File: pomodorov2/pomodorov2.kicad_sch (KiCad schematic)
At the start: 5 parts, among them J1 Conn_ARM_JTAG_SWD_10, J2 TC2050-IDC, J3 Conn_01x08, U1 nRF52832-QFxx

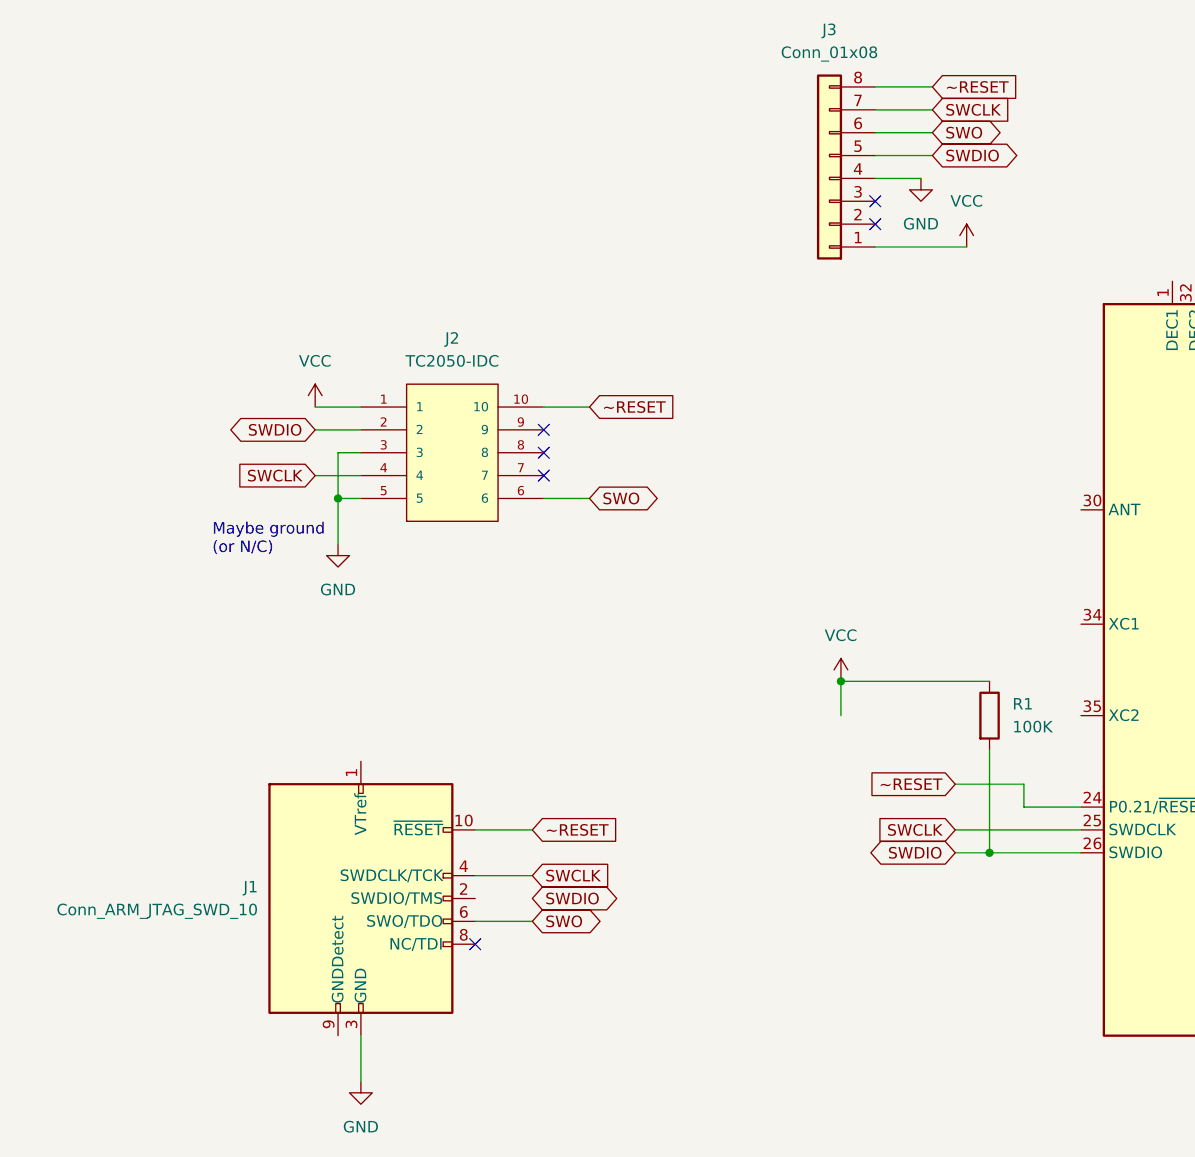
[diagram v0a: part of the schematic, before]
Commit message: Remove cortex header
- remove main cortex header
- tag-connect remains
- soicbite remains
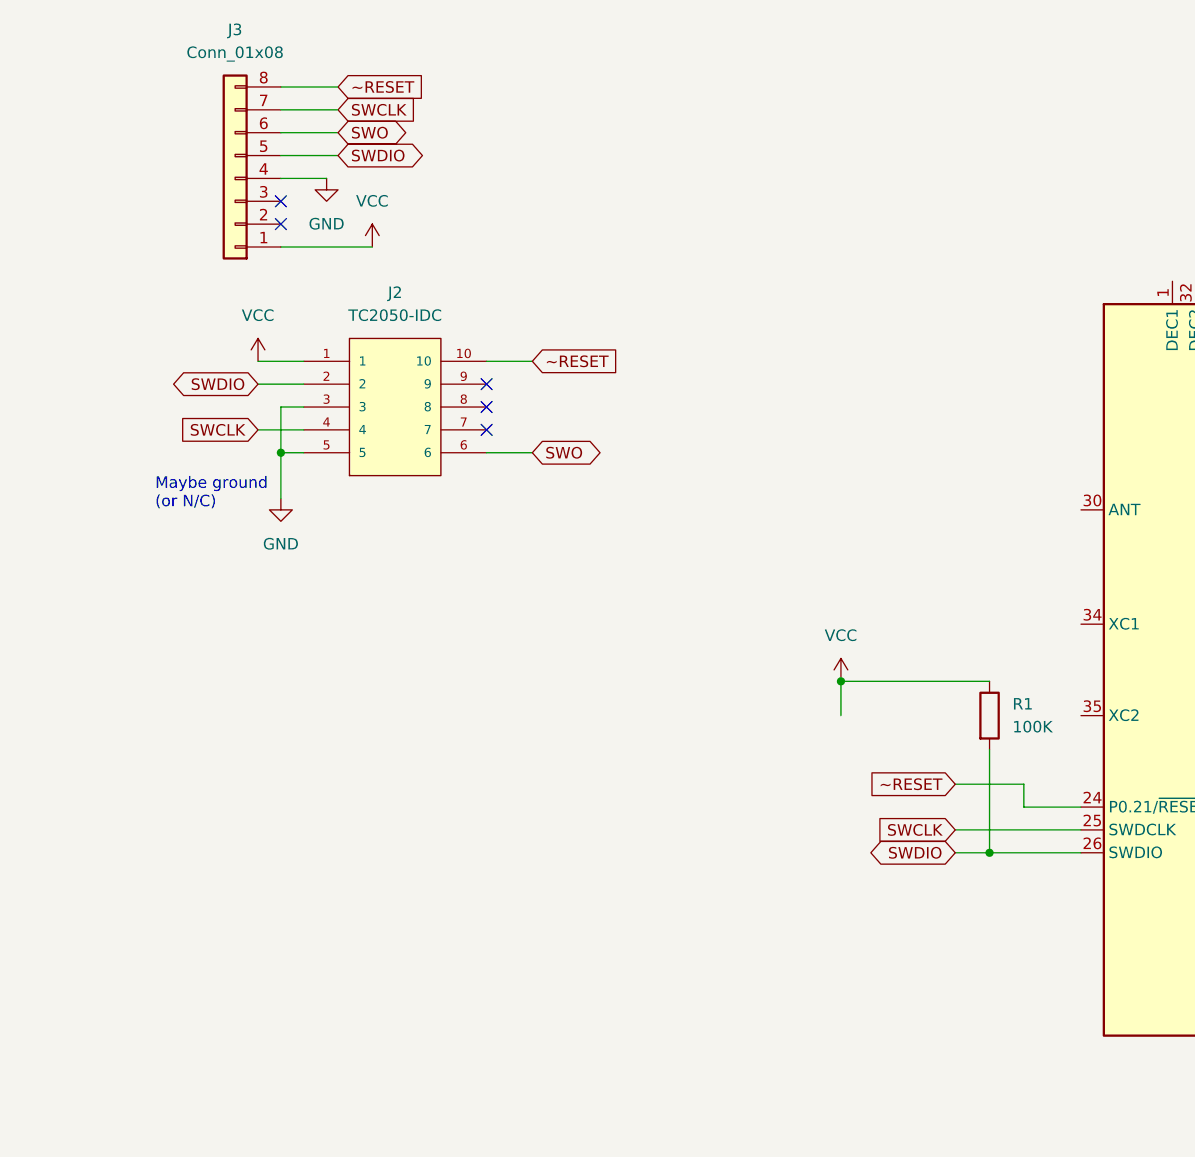
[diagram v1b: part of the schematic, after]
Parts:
- removed J1: Conn_ARM_JTAG_SWD_10, Connector_PinHeader_1.27mm:PinHeader_2x05_P1.27mm_Vertical_SMD, symbol Connector:Conn_ARM_JTAG_SWD_10
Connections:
- no-connect marks 6 -> 5
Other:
- moved on the sheet: J2, J3

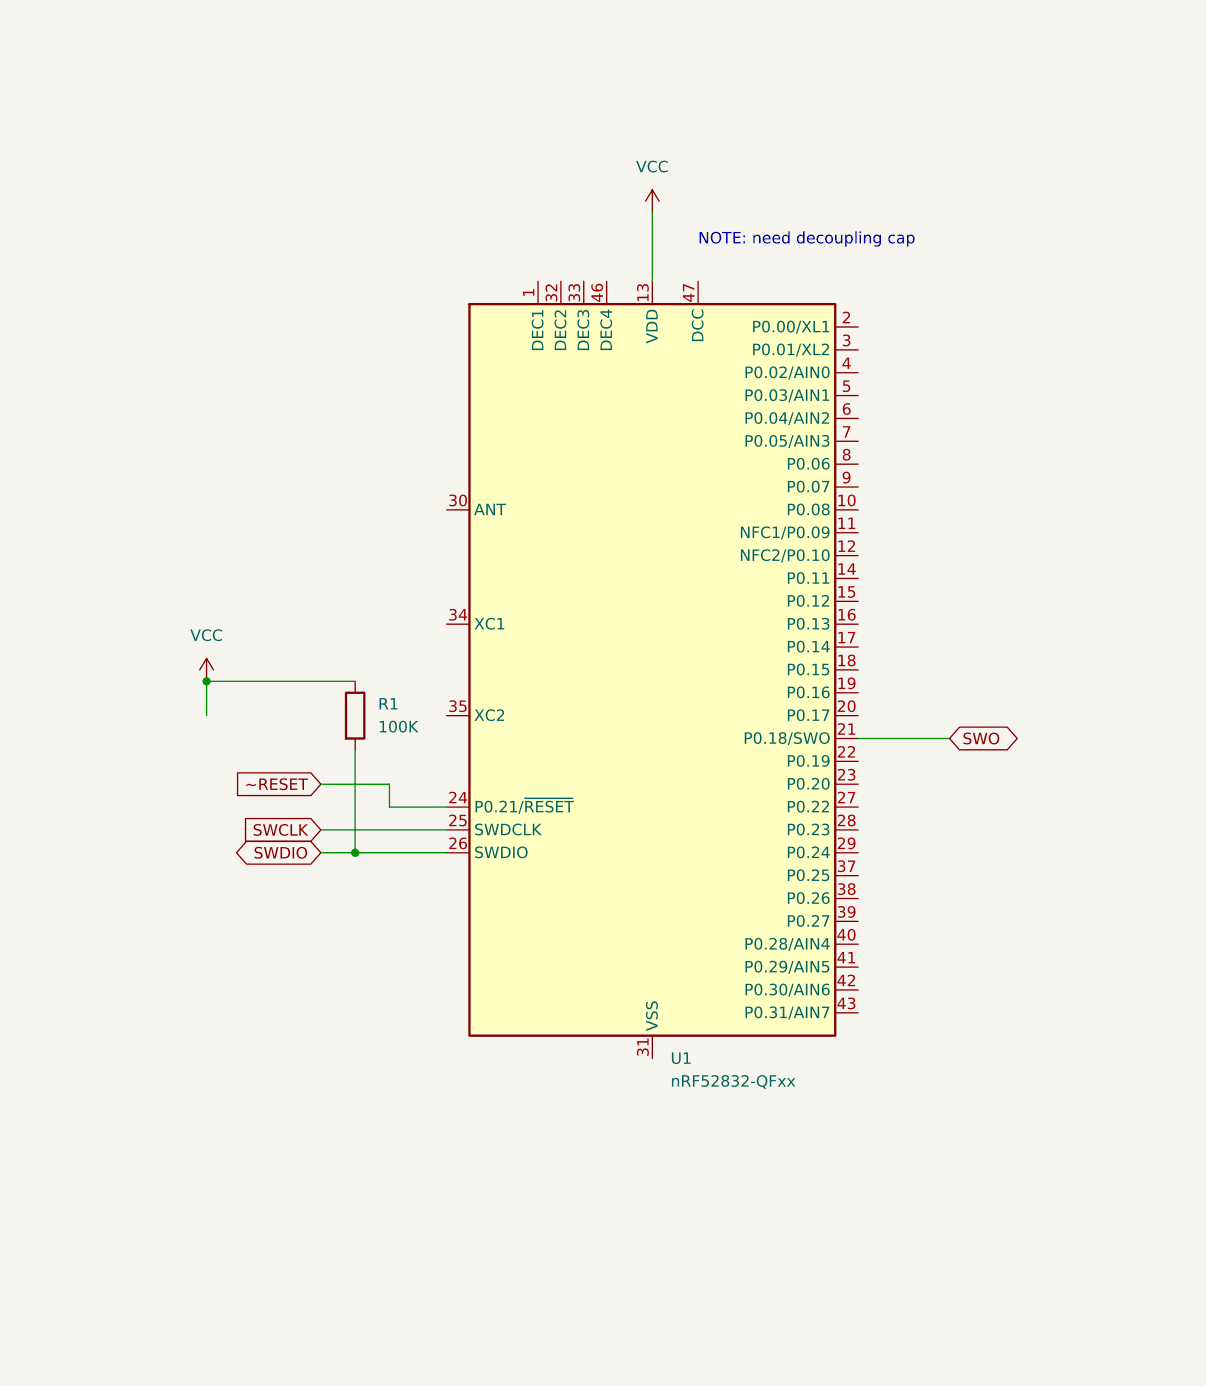
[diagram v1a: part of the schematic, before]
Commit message: Add components for chip, no routing 🚏
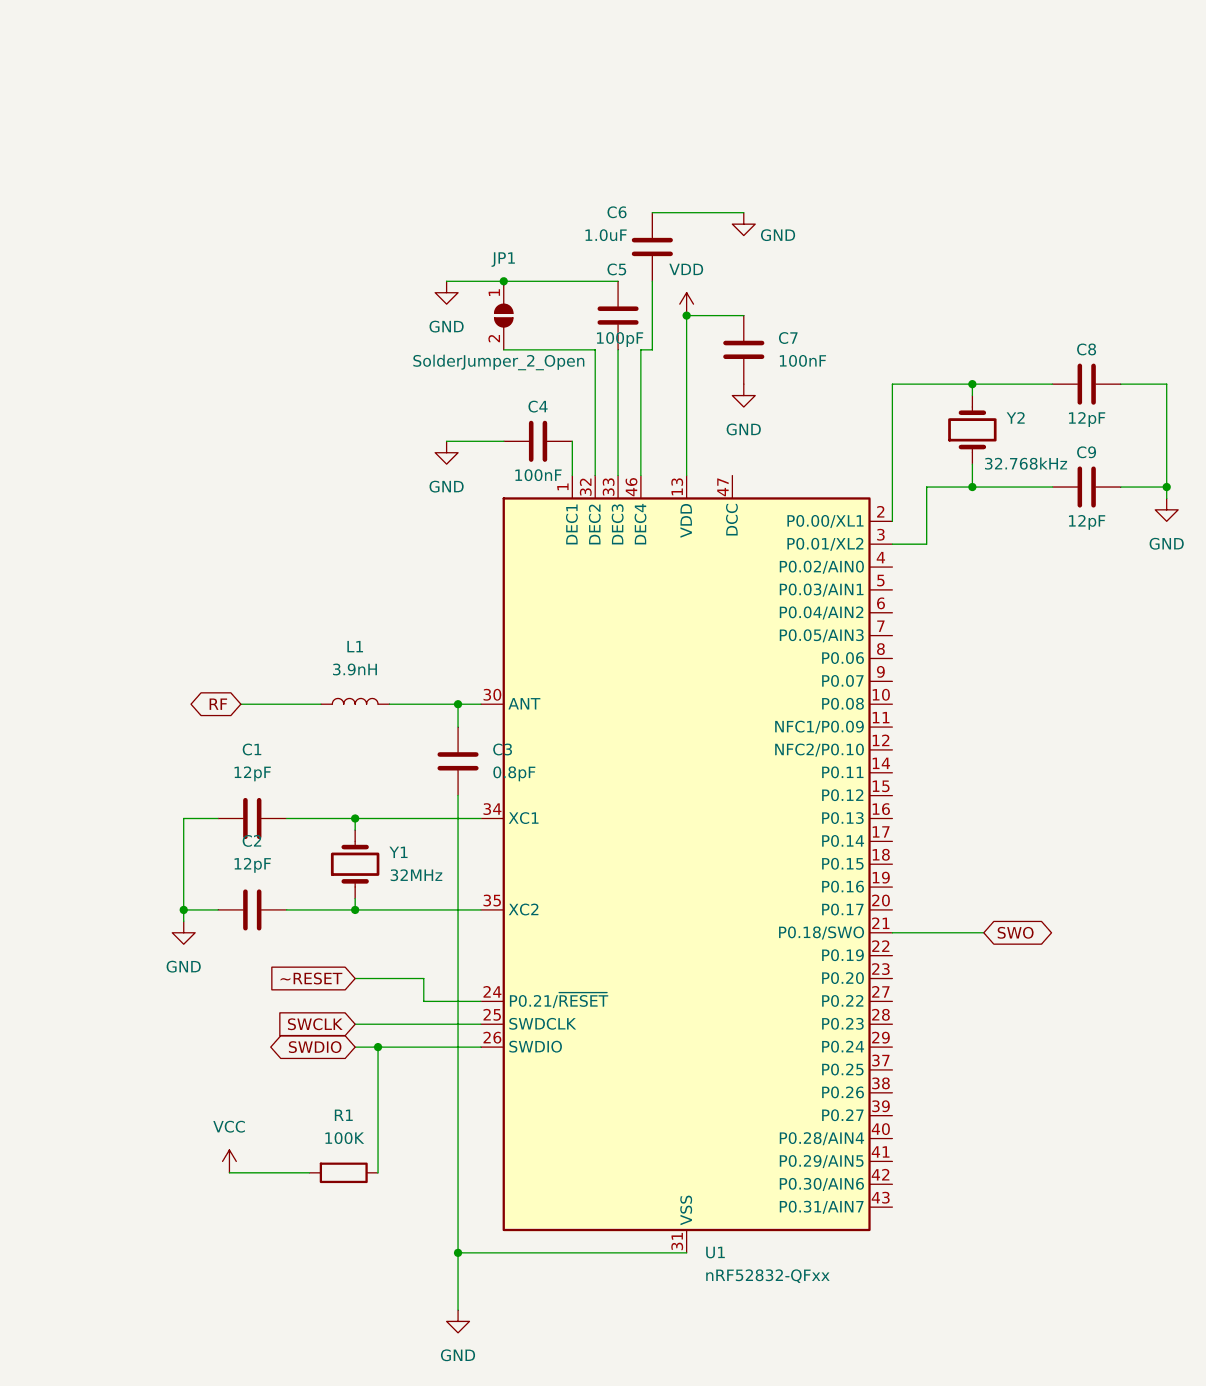
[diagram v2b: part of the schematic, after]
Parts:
- added C1, C2, C8, C9: 12pF, Capacitor_SMD:C_0805_2012Metric_Pad1.18x1.45mm_HandSolder, symbol Device:C
- added C3: 0.8pF, Capacitor_SMD:C_0805_2012Metric_Pad1.18x1.45mm_HandSolder, symbol Device:C
- added C4, C7: 100nF, Capacitor_SMD:C_0805_2012Metric_Pad1.18x1.45mm_HandSolder, symbol Device:C
- added C5: 100pF, Capacitor_SMD:C_0805_2012Metric_Pad1.18x1.45mm_HandSolder, symbol Device:C
- added C6: 1.0uF, Capacitor_SMD:C_0805_2012Metric_Pad1.18x1.45mm_HandSolder, symbol Device:C
- added JP1: SolderJumper_2_Open, Jumper:SolderJumper-2_P1.3mm_Open_TrianglePad1.0x1.5mm, symbol Jumper:SolderJumper_2_Open
- added L1: 3.9nH, Inductor_SMD:L_0805_2012Metric_Pad1.15x1.40mm_HandSolder, symbol Device:L
- added Y1: 32MHz, Crystal:Crystal_SMD_2016-4Pin_2.0x1.6mm, symbol Device:Crystal
- added Y2: 32.768kHz, Crystal:Crystal_SMD_3215-2Pin_3.2x1.5mm, symbol Device:Crystal
- J2: footprint TAG-CONNECT_TC2050-IDC -> TC2050-IDC:TAG-CONNECT_TC2050-IDC
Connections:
- net GND: now also U1.31 (VSS), U1.45 (VSS), U1.49 (VSS), C1.1, C2.1, C3.2, C4.1, C5.1, C6.1, C7.2, C8.2, C9.2, JP1.1 (A)
- net SWDIO: now also R1.1; no longer R1.2
- net VCC: now also R1.2; no longer R1.1, U1.13 (VDD), U1.36 (VDD), U1.48 (VDD)
- net at U1.1 (DEC1): now also C4.2
- net at U1.2 (P0.00/XL1): now also C8.1, Y2.2
- net at U1.3 (P0.01/XL2): now also C9.1, Y2.1
- net at U1.30 (ANT): now also C3.1, L1.2
- net at U1.32 (DEC2): now also JP1.2 (B)
- net at U1.33 (DEC3): now also C5.2
- net at U1.34 (XC1): now also C1.2, Y1.2
- net at U1.35 (XC2): now also C2.2, Y1.1
- net at U1.46 (DEC4): now also C6.2
- new net RF: L1.1
- new net VDD: C7.1, U1.13 (VDD), U1.36 (VDD), U1.48 (VDD)
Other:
- note removed: "NOTE: need decoupling cap"
- moved on the sheet: R1, U1
